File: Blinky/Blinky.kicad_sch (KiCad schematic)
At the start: 62 parts, among them J1 Conn_01x06_Socket, J2 Conn_01x06_Socket, J3 Battery Connector, J4 Charging Notches, Q1 IRLML6244, Q2 IRLML6244, Q3 IRLML6244, Q4 IRLML6244, Q5 IRLML6244, Q6 IRLML6244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

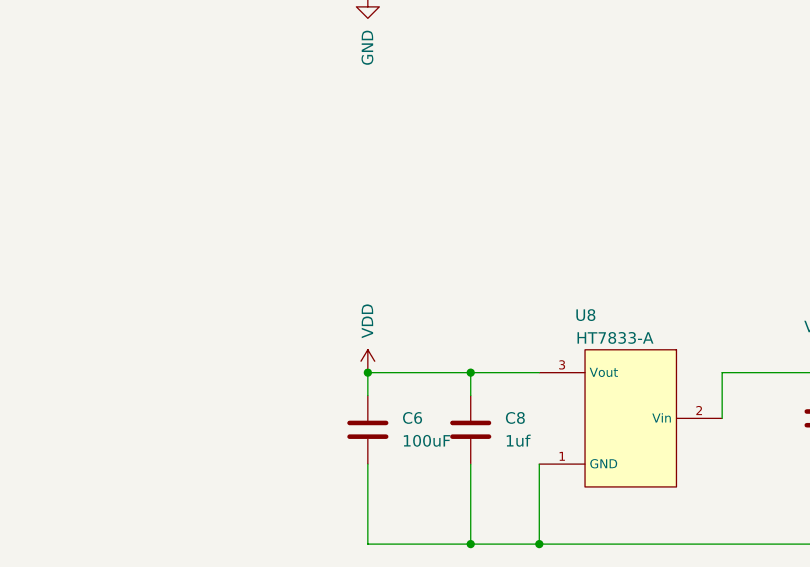
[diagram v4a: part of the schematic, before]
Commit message: added C after voltage reg
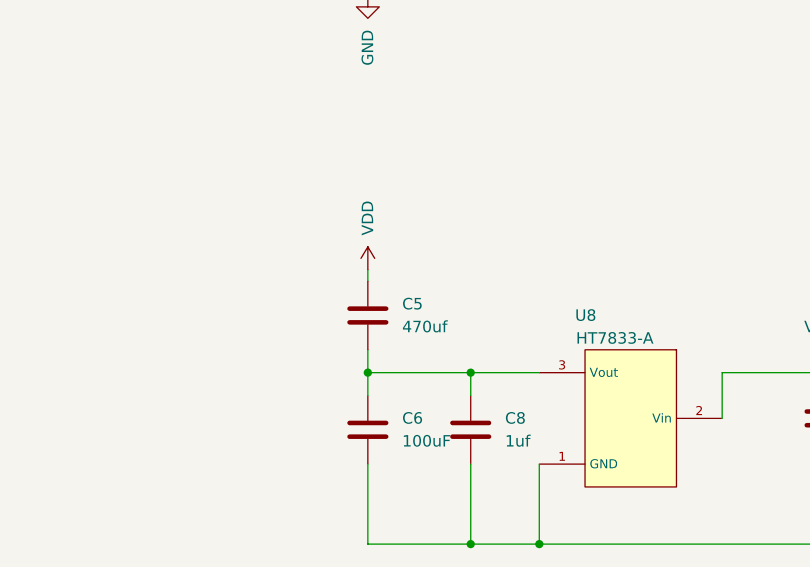
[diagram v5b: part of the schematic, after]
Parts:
- added C5: 470uf, Capacitor_SMD:C_0603_1608Metric, symbol Device:C
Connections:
- net VDD: now also C5.1; no longer C6.2, C8.2, U8.3 (Vout)
- new net: C5.2, C6.2, C8.2, U8.3 (Vout)
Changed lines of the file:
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@@
+    (stroke (width 0) (type default))
+  )
+  (wire (pts (xy 318.77 147.32) (xy 318.77 149.86))
     (stroke (width 0) (type default))
   )
@@
   )
   (wire (pts (xy 318.77 168.91) (xy 318.77 160.02))
+    (stroke (width 0) (type default))
+  )
+  (wire (pts (xy 318.77 138.43) (xy 318.77 139.7))
     (stroke (width 0) (type default))
   )
@@
     )
   )
-  (symbol (lib_id "power:VDD") (at 318.77 149.86 0) (unit 1)
-    (in_bom yes) (on_board yes) (dnp no)
-    (property "Reference" "#PWR032" (at 318.77 153.67 0)
-      (effects (font (size 1.27 1.27)) hide)
-    )
-    (property "Value" "VDD" (at 318.77 146.05 90)
+  (symbol (lib_id "power:VDD") (at 318.77 138.43 0) (unit 1)
+    (in_bom yes) (on_board yes) (dnp no)
+    (property "Reference" "#PWR032" (at 318.77 142.24 0)
+      (effects (font (size 1.27 1.27)) hide)
+    )
+    (property "Value" "VDD" (at 318.77 134.62 90)
       (effects (font (size 1.27 1.27)) (justify left))
     )
-    (property "Footprint" "" (at 318.77 149.86 0)
-      (effects (font (size 1.27 1.27)) hide)
-    )
-    (property "Datasheet" "" (at 318.77 149.86 0)
+    (property "Footprint" "" (at 318.77 138.43 0)
+      (effects (font (size 1.27 1.27)) hide)
+    )
+    (property "Datasheet" "" (at 318.77 138.43 0)
       (effects (font (size 1.27 1.27)) hide)
     )
@@
         )
       )
+    )
+  )
+  (symbol (lib_id "Device:C") (at 318.77 143.51 0) (unit 1)
+    (in_bom yes) (on_board yes) (dnp no) (fields_autoplaced)
+    (property "Reference" "C5" (at 322.58 142.24 0)
+      (effects (font (size 1.27 1.27)) (justify left))
+    )
+    (property "Value" "470uf" (at 322.58 144.78 0)
+      (effects (font (size 1.27 1.27)) (justify left))
+    )
+    (property "Footprint" "Capacitor_SMD:C_0603_1608Metric" (at 319.7352 147.32 0)
+      (effects (font (size 1.27 1.27)) hide)
+    )
+    (property "Datasheet" "~" (at 318.77 143.51 0)
+      (effects (font (size 1.27 1.27)) hide)
+    )
+    (pin "1")
+    (pin "2")
+    (instances
+      (project "Blinky"
+        (path "/a854b35b-60aa-44a5-a34e-fbb2d526cb93"
+          (reference "C5") (unit 1)
+        )
+      )

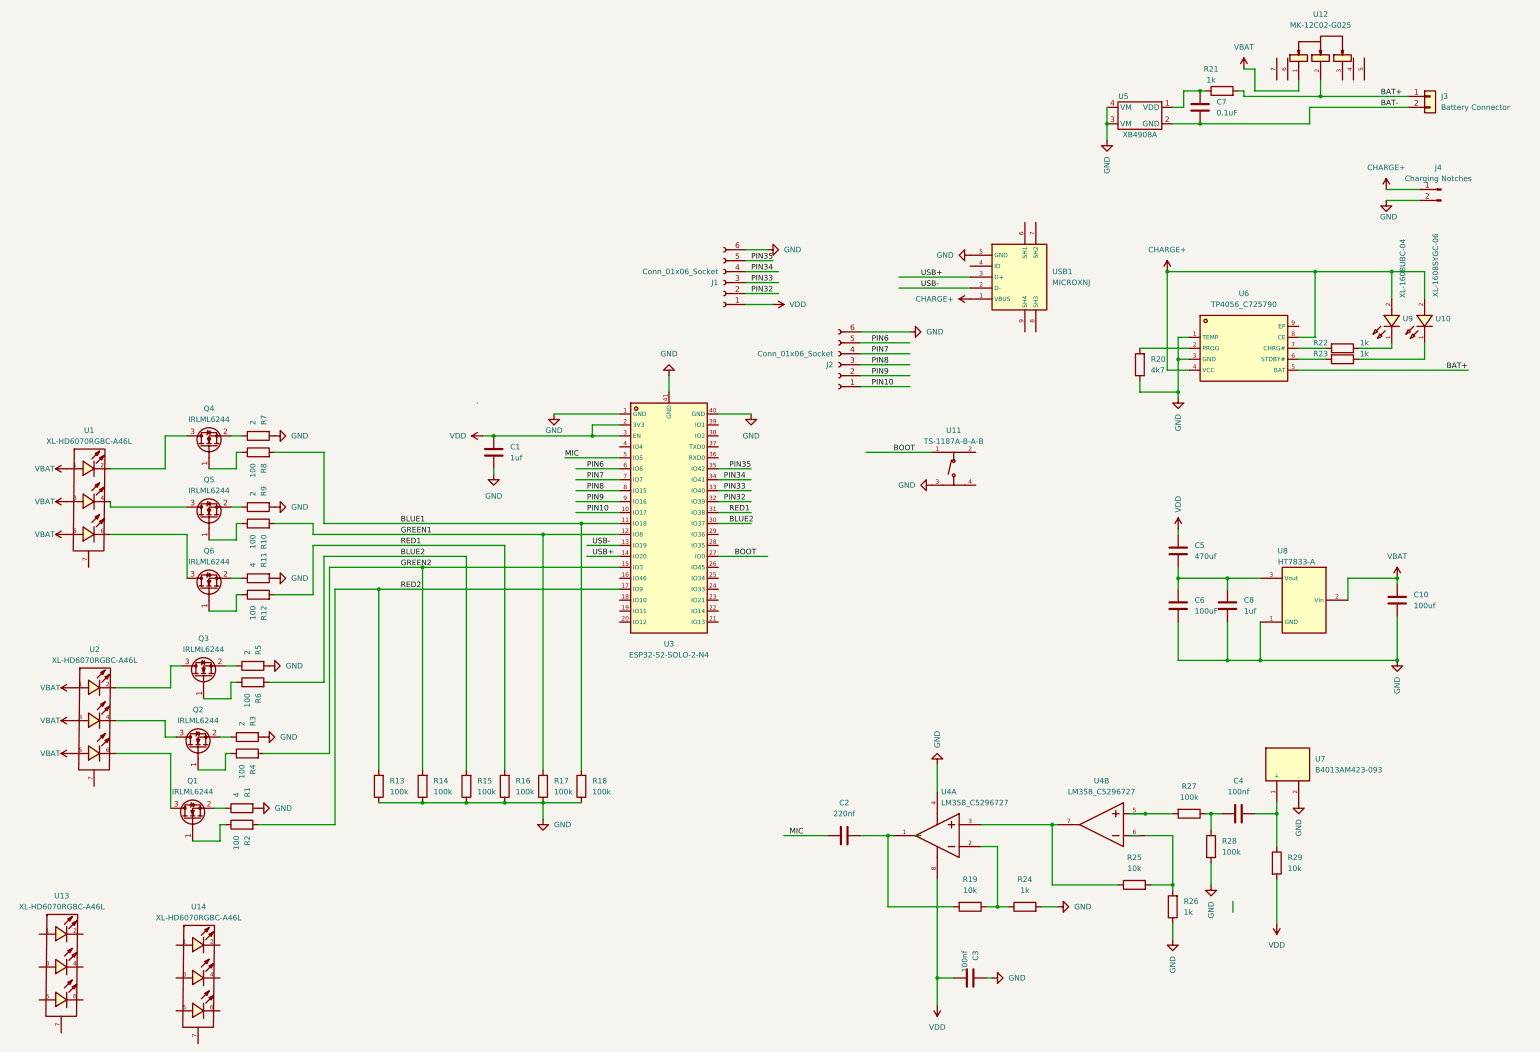
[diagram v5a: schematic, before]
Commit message: fixed Vreg and Mic
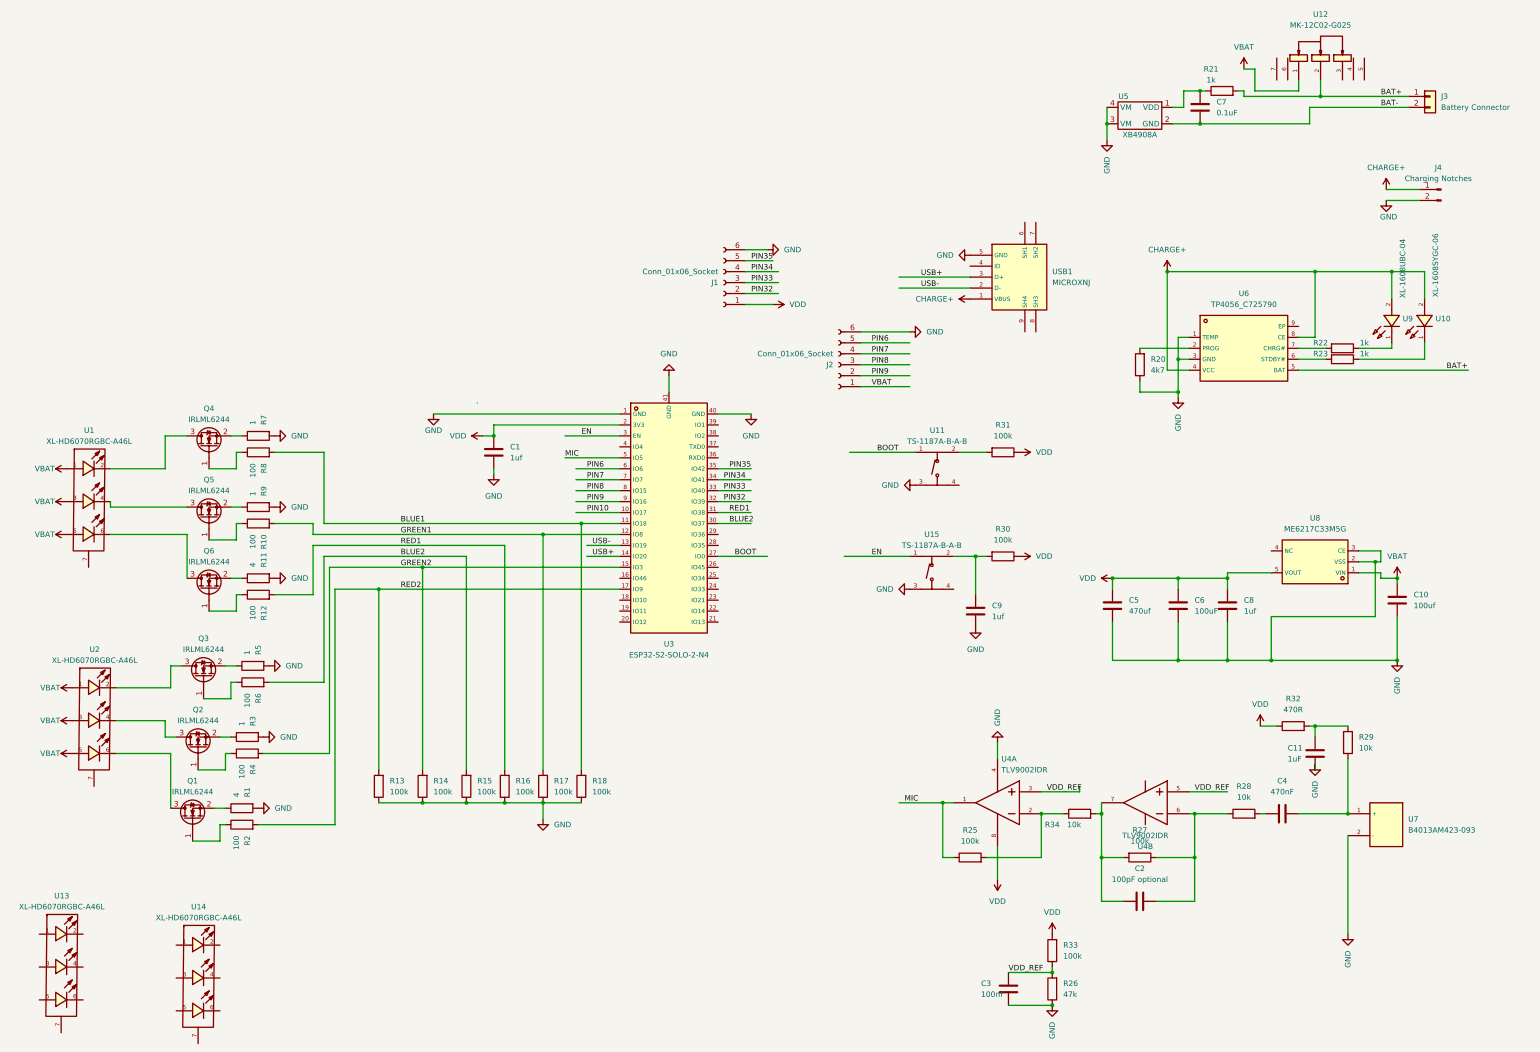
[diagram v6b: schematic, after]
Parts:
- removed R19: 10k, Resistor_SMD:R_0603_1608Metric, symbol Device:R
- removed R24: 1k, Resistor_SMD:R_0603_1608Metric, symbol Device:R
- removed U4: LM358_C5296727, footprint:SO-8_L4.9-W3.9-P1.27-LS6.0-BL, symbol LM358_C5296727:LM358_C5296727
- removed U8: HT7833-A, otherfootprint:SOT-89-3_L4.5-W2.5-P1.50-LS4.2-BR, symbol HT7533-1_C14289:HT7533-1_C14289
- added C11: 1uF, Capacitor_SMD:C_0603_1608Metric, symbol Device:C
- added C9: 1uf, Capacitor_SMD:C_0603_1608Metric, symbol Device:C
- added R30, R31, R33: 100k, Resistor_SMD:R_0603_1608Metric, symbol Device:R
- added R32: 470R, Resistor_SMD:R_0603_1608Metric, symbol Device:R
- added R34: 10k, Resistor_SMD:R_0603_1608Metric, symbol Device:R
- added U15: TS-1187A-B-A-B, footprint:SW-SMD_4P-L5.1-W5.1-P3.70-LS6.5-TL-2, symbol TS-1187A-B-A-B:TS-1187A-B-A-B
- added U4: TLV9002IDR, footprint:SOIC-8_L4.9-W3.9-P1.27-LS6.0-BL, symbol TLV9002IDR:TLV9002IDR
- added U8: ME6217C33M5G, footprint:SOT-23-5_L3.0-W1.7-P0.95-LS2.8-BR, symbol ME6217C33M5G:ME6217C33M5G
- C2: value 220nf -> 100pF optional
- C4: value 100nf -> 470nF
- R25: value 10k -> 100k
- R26: value 1k -> 47k
- R28: value 100k -> 10k
- R3, R5, R7, R9: value 2 -> 1
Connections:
- net GND: now also C3.2, C5.2, C11.2, C9.1, U15.3 (C), U4.4 (V-), U8.2 (VSS), U8.3 (CE); no longer C3.1, R28.2
- net MIC: now also R25.1, U4.1 (OUT1); no longer C2.1
- net PIN10: no longer J2.1 (Pin_1)
- net VBAT: now also J2.1 (Pin_1), U8.1 (VIN)
- net VDD: now also C6.2, C8.2, R30.1, R31.1, R32.1, R33.2, U4.8 (V+), U8.5 (VOUT); no longer C3.2, R29.2, U3.3 (EN)
- net at R27.2: now also C2.1, R34.2, U4.7 (OUT2)
- net at R25.2: now also R34.1, U4.2 (IN1-); no longer R26.2
- net at R27.1, R28.1: now also C2.2, U4.6 (IN2-); no longer C4.1
- net at C4.2, U7.1 (+): now also R29.2; no longer R29.1
- net at U11.2 (B): now also R31.2
- new net: C11.1, R29.1, R32.2
- new net: C4.1, R28.2
- new net: C9.2, R30.2, U15.2 (B)
- new net EN: U15.1 (A), U3.3 (EN)
- new net VDD_REF: C3.1, R26.2, R33.1, U4.3 (IN1+), U4.5 (IN2+)
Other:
- moved on the sheet: C3, C4, C5, R25, R26, R27, R28, R29, U11, U7

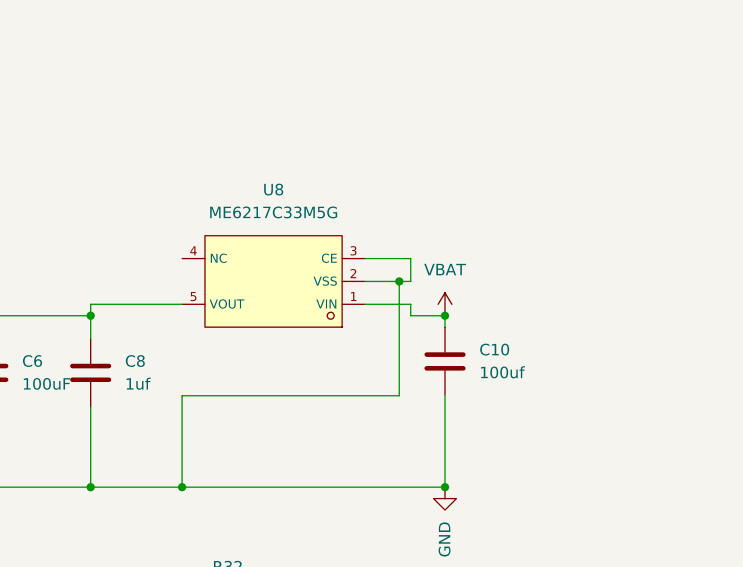
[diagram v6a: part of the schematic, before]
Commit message: fixed routing of u8 pin 3
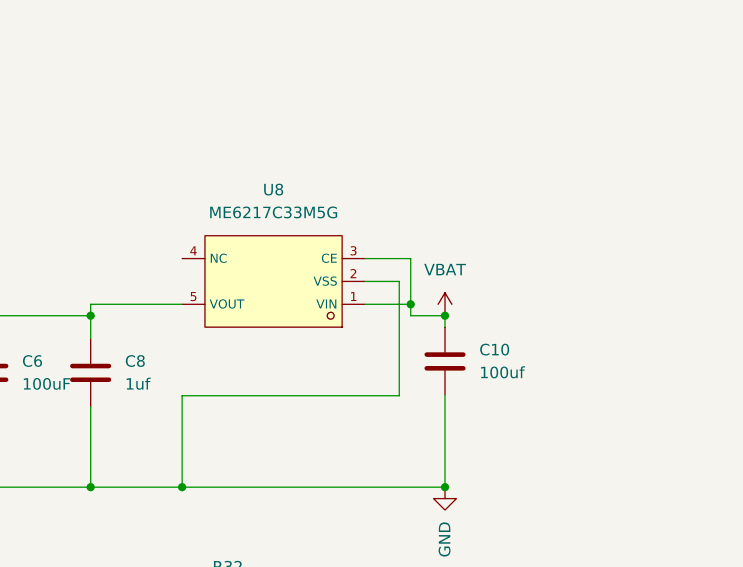
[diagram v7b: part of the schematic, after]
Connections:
- net GND: no longer U8.3 (CE)
- net VBAT: now also U8.3 (CE)
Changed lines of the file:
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@@
   (junction (at 368.3 78.74) (diameter 0) (color 0 0 0 0)
   )
+  (junction (at 365.76 148.59) (diameter 0) (color 0 0 0 0)
+  )
   (junction (at 323.85 44.45) (diameter 0) (color 0 0 0 0)
   )
@@
   (junction (at 302.26 44.45) (diameter 0) (color 0 0 0 0)
   )
-  (junction (at 364.49 146.05) (diameter 0) (color 0 0 0 0)
-  )
   (wire (pts (xy 316.23 78.74) (xy 350.52 78.74))
     (stroke (width 0) (type default))
@@
     (stroke (width 0) (type default))
   )
-  (wire (pts (xy 365.76 146.05) (xy 364.49 146.05))
-    (stroke (width 0) (type default))
-  )
   (wire (pts (xy 71.12 139.7) (xy 88.9 139.7))
     (stroke (width 0) (type default))
@@
     (stroke (width 0) (type default))
   )
-  (wire (pts (xy 365.76 143.51) (xy 365.76 146.05))
-    (stroke (width 0) (type default))
-  )
+  (wire (pts (xy 365.76 143.51) (xy 365.76 148.59))
+    (stroke (width 0) (type default))
+  )

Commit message: trying to fix C5
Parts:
- C1: value 1uf -> 47uf
- C6: value 100uF -> 10uf
- C8: value 1uf -> 100nf
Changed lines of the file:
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@@
       (effects (font (size 1.27 1.27)) (justify right))
     )
-    (property "Value" "100uF" (at 322.58 157.48 0)
+    (property "Value" "10uf" (at 322.58 157.48 0)
       (effects (font (size 1.27 1.27)) (justify right))
     )
@@
       (effects (font (size 1.27 1.27)) (justify right))
     )
-    (property "Value" "1uf" (at 163.83 121.92 0)
+    (property "Value" "47uf" (at 163.83 121.92 0)
       (effects (font (size 1.27 1.27)) (justify right))
     )
@@
       (effects (font (size 1.27 1.27)) (justify right))
     )
-    (property "Value" "1uf" (at 334.01 157.48 0)
-      (effects (font (size 1.27 1.27)) (justify right))
-    )
+    (property "Value" "100nf" (at 334.01 157.48 0)
+      (effects (font (size 1.27 1.27)) (justify right))
+    )
